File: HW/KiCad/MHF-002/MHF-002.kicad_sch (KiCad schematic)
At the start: 264 parts, among them J1 VGA, J10 I2C, J100 x, J101 x, J102 x, J103 x, J104 x, J105 x, J106 x, J107 +3V3, J108 GND, J109 +3V3, J11 + 5V -, J110 +5V, J111 GND, J112 GND, J12 Reset, J13 +5V, J14 GND, J15 AREF, J16 XTAL2, J17 SDcard, J18 XTAL1, J19 AVCC, J2 PS/2, J20 SDcardpins, J21 x, J22 x, J23 VIN 12V, J24 AND_B1, J25 AND_B2, J26 AND_C1, J27 AND_C2, J28 AND_D1, J29 AND_D2, J3 RCA, J30 AND_Dx, J31 AND_Cx, J32 AND_Bx, J33 NOTF, J34 NOTE, J35 NOTEx, J36 NOTFx, J37 x, J38 x, J39 x, J4 SysBus, J40 x, J41 x, J42 x, J43 x, J44 x, J45 x, J46 x, J47 x, J48 x, J49 x, J5 Micro, J50 x, J51 x, J52 x, J53 x, J54 x, J55 x, J56 x, J57 x, J58 x, J59 x, J6 SysBus, J60 x, J61 x, J62 x, J63 x, J64 x, J65 x, J66 x, J67 x, J68 x, J69 x, J7 SPI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

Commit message: external memory
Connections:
- net L4: now reaches M3.16 (A4), U6.12 (O4)
- net L5: now reaches M3.15 (A5), U6.15 (O5)
- net L6: now reaches M3.14 (A6), U6.16 (O6)
- net L7: now reaches M3.13 (A7), U6.19 (O7)
- net L3: now reaches M3.20 (A0), U6.2 (O0)
- net L2: now reaches M3.19 (A1), U6.5 (O1)
- net L1: now reaches M3.18 (A2), U6.6 (O2)
- net L0: now reaches M3.17 (A3), U6.9 (O3)
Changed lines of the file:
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@@
 	(wire
 		(pts
-			(xy 551.18 472.44) (xy 577.85 472.44)
+			(xy 551.18 472.44) (xy 769.62 472.44)
 		)
 		(stroke
@@
 	(wire
 		(pts
+			(xy 769.62 372.11) (xy 786.13 372.11)
+		)
+		(stroke
+			(width 0)
+			(type default)
+		)
+	)
+	(wire
+		(pts
 			(xy 472.44 347.98) (xy 478.79 347.98)
 		)
@@
 	(wire
 		(pts
-			(xy 783.59 372.11) (xy 786.13 372.11)
-		)
-		(stroke
-			(width 0)
-			(type default)
-		)
-	)
-	(wire
-		(pts
 			(xy 499.11 721.36) (xy 509.27 721.36)
 		)
@@
 	(wire
 		(pts
+			(xy 769.62 372.11) (xy 769.62 472.44)
+		)
+		(stroke
+			(width 0)
+			(type default)
+		)
+	)
+	(wire
+		(pts
 			(xy 763.27 367.03) (xy 786.13 367.03)
 		)
@@
 		)
 	)
+	(label "L7"
+		(at 763.27 349.25 0)
+		(effects
+			(font
+				(size 1.27 1.27)
+			)
+			(justify left bottom)
+		)
+	)
 	(label "A8"
 		(at 594.36 69.85 0)
@@
 		)
 	)
+	(label "L5"
+		(at 758.19 344.17 0)
+		(effects
+			(font
+				(size 1.27 1.27)
+			)
+			(justify left bottom)
+		)
+	)
 	(label "Shared_Address_A10"
 		(at 410.21 429.26 0)
@@
 		)
 	)
+	(label "L3"
+		(at 764.54 331.47 0)
+		(effects
+			(font
+				(size 1.27 1.27)
+			)
+			(justify left bottom)
+		)
+	)
 	(label "A_SHARE_GRANTED"
 		(at 689.61 88.9 0)
@@
 		)
 	)
+	(label "L6"
+		(at 762 346.71 0)
+		(effects
+			(font
+				(size 1.27 1.27)
+			)
+			(justify left bottom)
+		)
+	)
 	(label "A12"
 		(at 91.44 580.39 180)
@@
 		)
 	)
+	(label "L2"
+		(at 760.73 334.01 0)
+		(effects
+			(font
+				(size 1.27 1.27)
+			)
+			(justify left bottom)
+		)
+	)
 	(label "A12"
 		(at 594.36 74.93 0)
@@
 		)
 	)
+	(label "L0"
+		(at 753.11 339.09 0)
+		(effects
+			(font
+				(size 1.27 1.27)
+			)
+			(justify left bottom)
+		)
+	)
 	(label "A5"
 		(at 660.4 64.77 0)
@@
 		)
 	)
+	(label "L4"
+		(at 755.65 341.63 0)
+		(effects
+			(font
+				(size 1.27 1.27)
+			)
+			(justify left bottom)
+		)
+	)
 	(label "A16"
 		(at 689.61 78.74 0)
@@
 		(effects
 			(font
+				(size 1.27 1.27)
+			)
+			(justify left bottom)
+		)
+	)
+	(label "L1"
+		(at 756.92 336.55 0)
+		(effects
+			(font

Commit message: footprints for HandSoldering, some schema modifications
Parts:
- removed U4: 74HC165, Package_DIP:DIP-16_W7.62mm, symbol 74xx:74HC165
- added R44, R45: 10k, Resistor_SMD:R_0805_2012Metric_Pad1.20x1.40mm_HandSolder, symbol Device:R
- added U5: 74HC166, symbol 74xx:74LS166
- M3, M5: footprint Package_SO:TSOP-I-32_18.4x8mm_P0.5mm -> MHF:G_TSOP-I-32_18.4x8mm_HandSolder
- U1: footprint Package_QFP:TQFP-100_14x14mm_P0.5mm -> MHF:G_TQFP-100_14x14mm_HandSolder
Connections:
- net +5V: now also U5.16 (VCC), U5.9 (Clr)
- net 16MHz: now also U5.7 (Clk)
- net CTS: now also PB1.5 (Pin_5), U1.23 ((OC2A/PCINT4)PB4); no longer PE1.3 (Pin_3), U1.4 ((XCK0/AIN0)PE2)
- net GND: now also U5.6 (CE), U5.8 (GND)
- net PS2 Clock: now also R44.2; no longer JP56.2 (B)
- net PS2 Data: now also R45.2; no longer JP55.2 (B)
- net PS2-OE: now also PE1.3 (Pin_3), U1.4 ((XCK0/AIN0)PE2); no longer PB1.5 (Pin_5), U1.23 ((OC2A/PCINT4)PB4)
- net RTS: now also PB1.6 (Pin_6), U1.24 ((OC1A/PCINT5)PB5); no longer PE1.4 (Pin_4), U1.5 ((OC3A/AIN1)PE3)
- net Shared_data_D0: now also PL1.1 (Pin_1), U1.35 (PL0(ICP4)); no longer PF1.1 (Pin_1), U1.97 ((ADC0)PF0)
- net Shared_data_D1: now also PL1.2 (Pin_2), U1.36 (PL1(ICP5)); no longer PF1.2 (Pin_2), U1.96 ((ADC1)PF1)
- net Shared_data_D2: now also PL1.3 (Pin_3), U1.37 (PL2(T5)); no longer PF1.3 (Pin_3), U1.95 ((ADC2)PF2)
- net Shared_data_D3: now also PL1.4 (Pin_4), U1.38 (PL3(OC5A)); no longer PF1.4 (Pin_4), U1.94 ((ADC3)PF3)
- net Shared_data_D4: now also PL1.5 (Pin_5), U1.39 (PL4(OC5B)); no longer PF1.5 (Pin_5), U1.93 ((ADC4/TCK)PF4)
- net Shared_data_D5: now also PL1.6 (Pin_6), U1.40 (PL5(OC5C)); no longer PF1.6 (Pin_6), U1.92 ((ADC5/TMS)PF5)
- net Shared_data_D6: now also PL1.7 (Pin_7), U1.41 (PL6); no longer PF1.7 (Pin_7), U1.91 ((ADC6/TDO)PF6)
- net Shared_data_D7: now also PL1.8 (Pin_8), U1.42 (PL7); no longer PF1.8 (Pin_8), U1.90 ((ADC7/TDI)PF7)
- net VGA Latch: now also U5.15 (PE)
- net VGA data 0: now also PF1.1 (Pin_1), U1.97 ((ADC0)PF0), U5.2 (A); no longer PL1.1 (Pin_1), U1.35 (PL0(ICP4))
- net VGA data 1: now also PF1.2 (Pin_2), U1.96 ((ADC1)PF1), U5.3 (B); no longer PL1.2 (Pin_2), U1.36 (PL1(ICP5))
- net VGA data 2: now also PF1.3 (Pin_3), U1.95 ((ADC2)PF2), U5.4 (C); no longer PL1.3 (Pin_3), U1.37 (PL2(T5))
- net VGA data 3: now also PF1.4 (Pin_4), U1.94 ((ADC3)PF3), U5.5 (D); no longer PL1.4 (Pin_4), U1.38 (PL3(OC5A))
- net VGA data 4: now also PF1.5 (Pin_5), U1.93 ((ADC4/TCK)PF4), U5.10 (E); no longer N1.2, PL1.5 (Pin_5), U1.39 (PL4(OC5B))
- net VGA data 5: now also PF1.6 (Pin_6), U1.92 ((ADC5/TMS)PF5), U5.11 (F); no longer PL1.6 (Pin_6), U1.40 (PL5(OC5C))
- net VGA data 6: now also PF1.7 (Pin_7), U1.91 ((ADC6/TDO)PF6), U5.12 (G); no longer PL1.7 (Pin_7), U1.41 (PL6)
- net VGA data 7: now also PF1.8 (Pin_8), U1.90 ((ADC7/TDI)PF7), U5.14 (H); no longer PL1.8 (Pin_8), U1.42 (PL7)
- net VSyncVGA: now also N1.2
- net X16: now also PE1.4 (Pin_4), U1.5 ((OC3A/AIN1)PE3); no longer PB1.6 (Pin_6), U1.24 ((OC1A/PCINT5)PB5)
- net at U9.1 (S): now also U5.13 (Qh)
- new net: JP55.2 (B), R45.1
- new net: JP56.2 (B), R44.1
- no-connect marks 120 -> 119
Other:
- note added: "PB7 is usual Arduino Mega SYSTEM_LED - with VGA it will shine full time"
- moved on the sheet: C5, J15, U2E

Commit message: +footprints
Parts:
- added JP15: TX340, Jumper:SolderJumper-2_P1.3mm_Open_RoundedPad1.0x1.5mm, symbol Jumper:SolderJumper_2_Open
- added JP16: RX340, Jumper:SolderJumper-2_P1.3mm_Open_RoundedPad1.0x1.5mm, symbol Jumper:SolderJumper_2_Open
- added JP17: CTS340, Jumper:SolderJumper-2_P1.3mm_Open_RoundedPad1.0x1.5mm, symbol Jumper:SolderJumper_2_Open
- added JP18: DTR340, Jumper:SolderJumper-2_P1.3mm_Open_RoundedPad1.0x1.5mm, symbol Jumper:SolderJumper_2_Open
- added JP19: RTS340, Jumper:SolderJumper-2_P1.3mm_Open_RoundedPad1.0x1.5mm, symbol Jumper:SolderJumper_2_Open
- added JP20: USB_GND, MHF:G_rework_jumper_2.54mm, symbol MHF:ReworkJumper_2_Bridged
- added M1: CP2102, MHF:G_CP2102, symbol MHF:G_CP2102
- C9: footprint Capacitor_SMD:C_0603_1608Metric_Pad1.08x0.95mm_HandSolder -> Capacitor_THT:C_Disc_D3.0mm_W2.0mm_P2.50mm
- J2: footprint other.pretty:J_Mini-DIN-6 -> MHF:J_Mini-DIN-6; symbol Connector:Mini-DIN-6 -> MHF:Mini-DIN-6
- J3: footprint Gilhad:CUI_RCJ-047_Yellow -> MHF:CUI_RCJ-047_Yellow; symbol Connector:Conn_Coaxial -> MHF:Conn_Coaxial
- U10, U11, U12: footprint Package_SO:SOIC-20W_7.5x12.8mm_P1.27mm -> MHF:G_SOIC-20W_7.5x12.8mm_P1.27mm_HandSolder
- U5: footprint (none) -> MHF:G_SOIC-16_3.9x9.9mm_HandSolder
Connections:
- net CTS: now also JP17.2 (B); no longer U13.9 (~{CTS})
- net GND: now also JP20.2 (B); no longer J5.5 (GND), J5.6 (Shield)
- net M8RXD: now also JP16.2 (B); no longer U13.3 (RXD)
- net M8TXD: now also JP15.2 (B); no longer U13.2 (TXD)
- net RTS: now also JP19.2 (B); no longer U13.14 (~{RTS})
- net at C9.2, R28.2: now also JP18.2 (B); no longer U13.13 (~{DTR})
- new net: JP18.1 (A), U13.13 (~{DTR})
- new net: J5.5 (GND), J5.6 (Shield), JP20.1 (A)
- new net: JP17.1 (A), U13.9 (~{CTS})
- new net: JP15.1 (A), U13.2 (TXD)
- new net: JP19.1 (A), U13.14 (~{RTS})
- new net: JP16.1 (A), U13.3 (RXD)

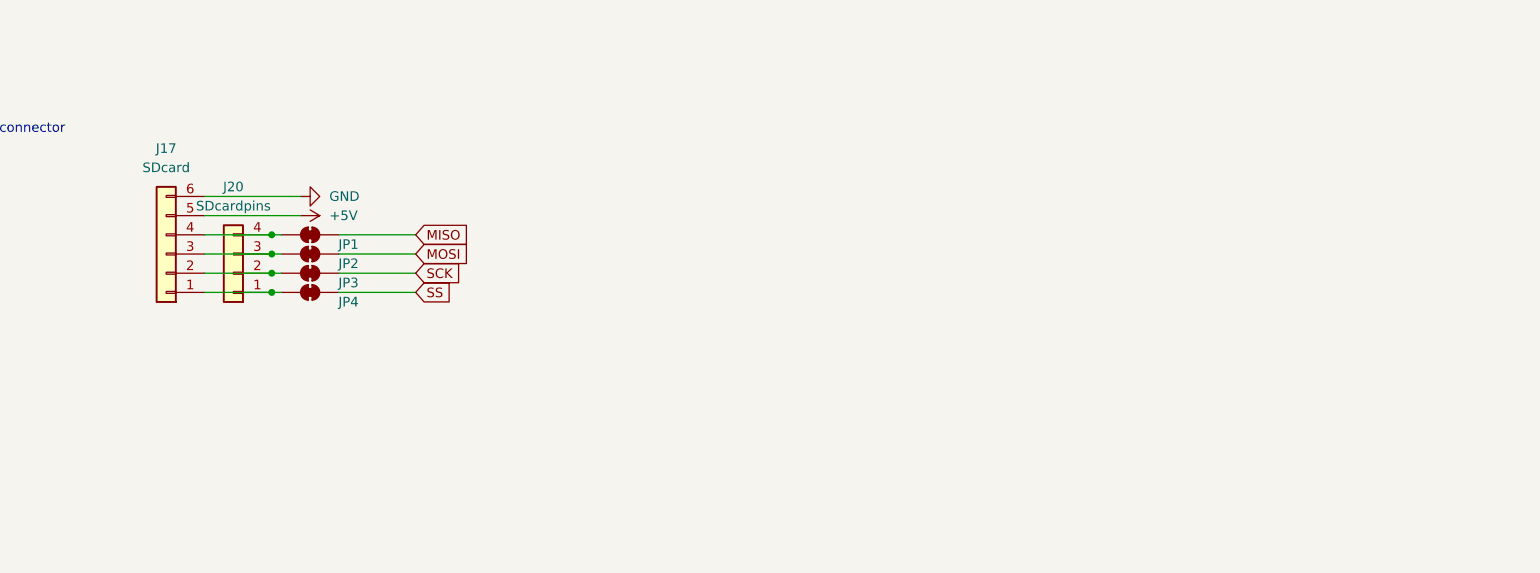
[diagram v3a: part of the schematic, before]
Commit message: +cp2102 +SDCard
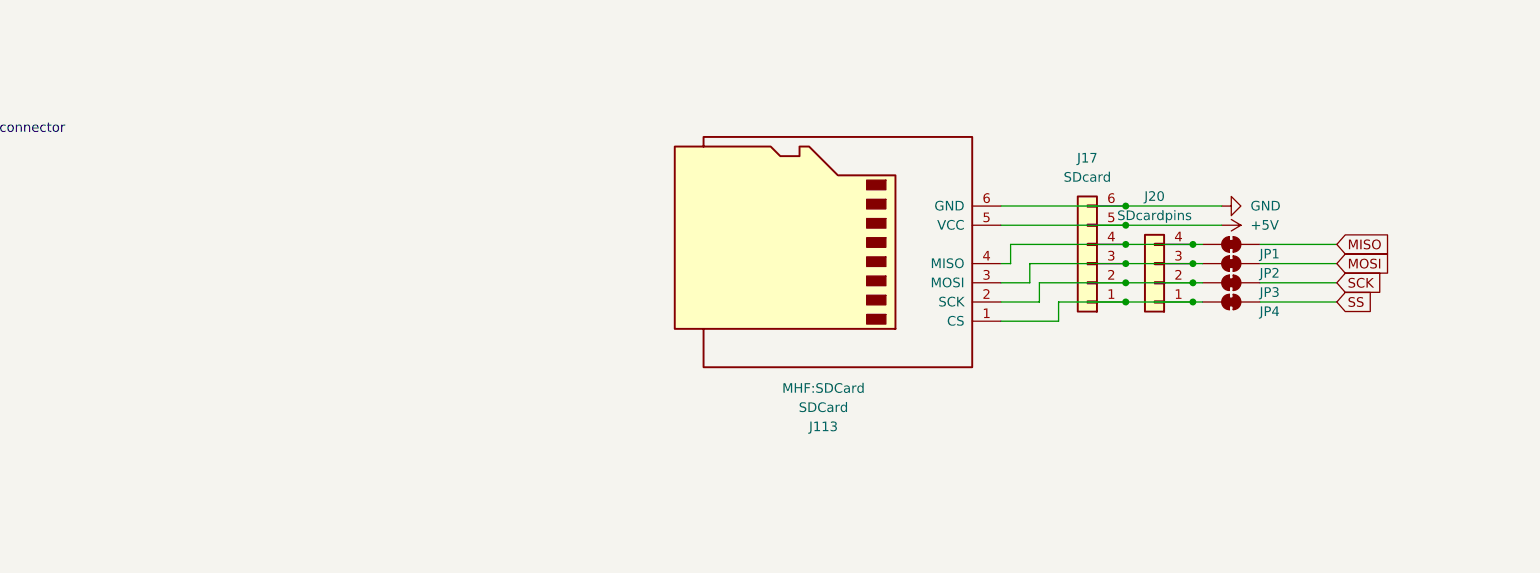
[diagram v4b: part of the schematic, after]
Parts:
- added J113: SDCard, MHF:SDCard, symbol MHF:SDCard
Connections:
- net +5V: now also J113.5 (VCC)
- net GND: now also J113.6 (GND)
- net at J17.3 (Pin_3), J20.3 (Pin_3), JP2.1 (A): now also J113.3 (MOSI)
- net at J17.4 (Pin_4), J20.4 (Pin_4), JP1.1 (A): now also J113.4 (MISO)
- net at J17.1 (Pin_1), J20.1 (Pin_1), JP4.1 (A): now also J113.1 (CS)
- net at J17.2 (Pin_2), J20.2 (Pin_2), JP3.1 (A): now also J113.2 (SCK)
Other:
- moved on the sheet: J17, J20, JP1, JP2, JP3, JP4

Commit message: more small fixes
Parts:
- removed U6: 74AHC373, Package_SO:TSSOP-20_4.4x6.5mm_P0.65mm, symbol 74xx:74AHC373
- added JP21: TX2102, Jumper:SolderJumper-2_P1.3mm_Open_RoundedPad1.0x1.5mm, symbol Jumper:SolderJumper_2_Open
- added JP22: RX2102, Jumper:SolderJumper-2_P1.3mm_Open_RoundedPad1.0x1.5mm, symbol Jumper:SolderJumper_2_Open
- added JP23: CTS2102, Jumper:SolderJumper-2_P1.3mm_Open_RoundedPad1.0x1.5mm, symbol Jumper:SolderJumper_2_Open
- added JP24: DTR2102, Jumper:SolderJumper-2_P1.3mm_Open_RoundedPad1.0x1.5mm, symbol Jumper:SolderJumper_2_Open
- added JP25: RTS2102, Jumper:SolderJumper-2_P1.3mm_Open_RoundedPad1.0x1.5mm, symbol Jumper:SolderJumper_2_Open
- added JP26: PS/2, Connector_PinHeader_2.54mm:PinHeader_1x02_P2.54mm_Vertical, symbol Connector_Generic:Conn_01x02
- added JP27: VGA, Connector_PinHeader_2.54mm:PinHeader_1x06_P2.54mm_Vertical, symbol Connector_Generic:Conn_01x06
- added JP28: RCA, Connector_PinHeader_2.54mm:PinHeader_1x02_P2.54mm_Vertical, symbol Connector_Generic:Conn_01x02
- added U4: 74AHC573, Package_SO:TSSOP-20_4.4x5mm_P0.5mm, symbol 74xx:74LS573
- C1: value 100 pF -> 10 nF
- J113: footprint MHF:SDCard -> SDCard:SDCard
- Q1: value BC107 -> S8050
- R1: value 3k3/22k -> 20k
- S1: symbol Arduino Mega 2560:TS06-667-30-BK-100-G-SMT-TR -> Switch:SW_MEC_5E
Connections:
- net +5V: now also M1.8 (+5V), U4.20 (VCC)
- net ALE: now also U4.11 (Load)
- net Blue: now also JP27.3 (Pin_3)
- net CTS: now also JP23.2 (B)
- net GND: now also M1.9 (GND), S1.3 (K), S1.4 (A), JP27.6 (Pin_6), JP28.2 (Pin_2), U4.1 (OE), U4.10 (GND); no longer S1.1, S1.2, S1.5
- net Green: now also JP27.4 (Pin_4)
- net L0: now also U4.16 (Q3)
- net L1: now also U4.17 (Q2)
- net L2: now also U4.18 (Q1)
- net L3: now also U4.19 (Q0)
- net L4: now also U4.15 (Q4)
- net L5: now also U4.14 (Q5)
- net L6: now also U4.13 (Q6)
- net L7: now also U4.12 (Q7)
- net M8RXD: now also JP22.2 (B)
- net M8TXD: now also JP21.2 (B)
- net PS2 Data: now also JP26.2 (Pin_2)
- net RCA_Output: now also JP28.1 (Pin_1)
- net RTS: now also JP25.2 (B)
- net Red: now also JP27.5 (Pin_5)
- net Reset: now also S1.1, S1.2; no longer S1.3, S1.4
- net XAD0: now also U4.5 (D3)
- net XAD1: now also U4.4 (D2)
- net XAD2: now also U4.3 (D1)
- net XAD3: now also U4.2 (D0)
- net XAD4: now also U4.6 (D4)
- net XAD5: now also U4.7 (D5)
- net XAD6: now also U4.8 (D6)
- net XAD7: now also U4.9 (D7)
- net at J1.13, R14.1: now also JP27.2 (Pin_2)
- net at J1.14, R15.1: now also JP27.1 (Pin_1)
- net DTR: now reaches C9.2, JP18.2 (B), R28.2
- net DTR: now also JP24.2 (B)
- net at M1.3 (RTS): now also JP25.1 (A)
- net at M1.4 (CTS): now also JP23.1 (A)
- net at M1.5 (DTR): now also JP24.1 (A)
- net at M1.6 (RXD): now also JP22.1 (A)
- net at M1.7 (TXD): now also JP21.1 (A)
- net at J2.5, R13.1, U2.1: now also JP26.1 (Pin_1)
- no-connect marks 119 -> 126
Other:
- moved on the sheet: C12, C9, D2, J113, J12, R14, R15, R26, R28

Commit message: +Switch
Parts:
- added LED10: Reset, LED_SMD:LED_0805_2012Metric, symbol Device:LED
- added LED9: SYSTEM, LED_SMD:LED_0805_2012Metric, symbol Device:LED
- added R46, R47: 10k, Resistor_SMD:R_0805_2012Metric_Pad1.20x1.40mm_HandSolder, symbol Device:R
- C12: footprint Capacitor_SMD:C_0603_1608Metric_Pad1.08x0.95mm_HandSolder -> Capacitor_THT:C_Disc_D3.0mm_W2.0mm_P2.50mm
- C13, C14: value 100n -> 22p
- J113: footprint SDCard:SDCard -> MHF:SDCard
- JP20: footprint MHF:G_rework_jumper_2.54mm -> MHF:G_Rework_Jumper_Bridged_2.54mm; symbol MHF:ReworkJumper_2_Bridged -> MHF:Rework_Jumper_2_Bridged
- S1: footprint Arduino Mega 2560:SW_TS06-667-30-BK-100-G-SMT-TR -> MHF:G_Arduino_switch; symbol Switch:SW_MEC_5E -> MHF:Arduino_Switch
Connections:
- net +5V: now also R47.2
- net GND: now also LED9.1 (K)
- net Reset: now also LED10.1 (K)
- net VGA Latch: now also R46.2
- new net: LED10.2 (A), R47.1
- new net: LED9.2 (A), R46.1

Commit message: fixing small problems
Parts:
- added JP30: USB_PWR, MHF:G_Rework_Jumper_Bridged_2.54mm, symbol MHF:Rework_Jumper_2_Bridged
- added JP31: USB_D+, MHF:G_Rework_Jumper_Bridged_2.54mm, symbol MHF:Rework_Jumper_2_Bridged
- added JP32: USB_D-, MHF:G_Rework_Jumper_Bridged_2.54mm, symbol MHF:Rework_Jumper_2_Bridged
- C1, C10, C11, C12, C13, C14, C15, C16, C2, C3, C4, C5, C6, C7, C8, C9, Cx1, Cx10, Cx11, Cx12, Cx13, Cx2, Cx3, Cx4, Cx5, Cx6, Cx7, Cx8, Cx9: symbol Device:C -> MHF:C
- Cx14, Cx15: symbol Device:C_Polarized -> MHF:C_Polarized
- D1: symbol Diode:1N4001 -> MHF:1N4001
- D2, D3: symbol Device:D -> MHF:D
- F1: symbol Device:Polyfuse -> MHF:Polyfuse
- H5, H6, H7, H8: symbol Mechanical:MountingHole -> MHF:MountingHole
- J1: symbol Connector:DE15_Socket_HighDensity_MountingHoles -> MHF:DE15_Socket_HighDensity_MountingHoles
- J10, J20: symbol Connector_Generic:Conn_01x04 -> MHF:Conn_01x04
- J100, J101, J102, J103, J104, J105, J106, J107, J108, J109, J110, J111, J112, J12, J13, J14, J15, J16, J18, J19, J21, J22, J24, J25, J26, J27, J28, J29, J30, J31, J32, J33, J34, J35, J36, J37, J38, J39, J40, J41, J42, J43, J44, J45, J46, J47, J48, J49, J50, J51, J52, J53, J54, J55, J56, J57, J58, J59, J60, J61, J62, J63, J64, J65, J66, J67, J68, J69, J70, J71, J72, J73, J74, J75, J76, J77, J78, J79, J80, J81, J82, J83, J84, J85, J86, J87, J88, J89, J90, J91, J92, J93, J94, J95, J96, J97, J98, J99: symbol PCM_Gilhad_symbols:Conn_01x01 -> MHF:Conn_01x01
- J11: symbol Connector_Generic:Conn_02x03_Odd_Even -> MHF:Conn_02x03_Odd_Even
- J17, J7, J9, JP27, PG1: symbol Connector_Generic:Conn_01x06 -> MHF:Conn_01x06
- J23: symbol Connector:Barrel_Jack_Switch -> MHF:Barrel_Jack_Switch
- J4, J6: symbol Connector_Generic:Conn_02x32_Odd_Even -> MHF:Conn_02x32_Odd_Even
- J5: symbol Connector:USB_B_Micro -> MHF:USB_B_Micro
- J8: symbol Connector:AVR-ISP-6 -> MHF:AVR-ISP-6
- JP1, JP10, JP11, JP12, JP13, JP14, JP2, JP3, JP4, JP5, JP6, JP7, JP8, JP9, JP91: symbol Jumper:SolderJumper_2_Bridged -> MHF:SolderJumper_2_Bridged
- JP100, JP102, JP103, JP104, JP105, JP106, JP107, JP92, JP94, JP95, JP98, JP99: symbol Jumper:SolderJumper_3_Open -> MHF:SolderJumper_3_Open
- JP15, JP16, JP17, JP18, JP19, JP21, JP22, JP23, JP24, JP25, JP55, JP56: symbol Jumper:SolderJumper_2_Open -> MHF:SolderJumper_2_Open
- JP26, JP28: symbol Connector_Generic:Conn_01x02 -> MHF:Conn_01x02
- LED1, LED10, LED2, LED3, LED4, LED5, LED6, LED7, LED8, LED9: symbol Device:LED -> MHF:LED
- M3, M5: symbol Memory_RAM:AS6C1008-xxST -> MHF:AS6C1008-xxST
- N1, N3: symbol Device:NetTie_2 -> MHF:NetTie_2
- PA1, PB1, PC1, PD1, PE1, PF1, PH1, PJ1, PK1, PL1: symbol Connector_Generic:Conn_01x08 -> MHF:Conn_01x08
- Q1: symbol Transistor_BJT:S8050 -> MHF:S8050
- R1, R10, R11, R12, R13, R14, R15, R16, R17, R18, R19, R2, R20, R21, R22, R23, R24, R25, R26, R27, R28, R29, R3, R30, R31, R32, R33, R34, R35, R36, R37, R38, R39, R4, R40, R41, R42, R43, R44, R45, R46, R47, R5, R6, R7, R8, R9: symbol Device:R -> MHF:R
- U1: symbol Arduino Mega 2560:ATMEGA2560-16AU -> MHF:ATMEGA2560-16AU
- U10, U11, U12: symbol 74xx:74HC245 -> MHF:74HC245
- U13: symbol Interface_USB:CH340G -> MHF:CH340G
- U14: symbol Regulator_Linear:AMS1117-5.0 -> MHF:AMS1117-5.0
- U15: symbol Regulator_Linear:AMS1117-3.3 -> MHF:AMS1117-3.3
- U2: symbol 74xx:74HC14 -> MHF:74HC14
- U3: value 74LS08 -> 74HC08; symbol 74xx:74LS08 -> MHF:74HC08
- U4: symbol 74xx:74LS573 -> MHF:74HC573
- U5: symbol 74xx:74LS166 -> MHF:74HC166
- U7, U8: symbol 74xx:74HCT595 -> MHF:74HC595
- U9: symbol 74xx:74LS157 -> MHF:74HC157
- Y1, Y2: symbol Device:Crystal -> MHF:Crystal
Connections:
- net at R24.2: now also JP31.2 (B); no longer J5.3 (D+)
- net at J5.1 (VBUS): now also JP30.1 (A); no longer F1.2
- net at J5.2 (D-): now also JP32.1 (A); no longer R25.2
- new net: JP32.2 (B), R25.2
- new net: F1.2, JP30.2 (B)
- new net: J5.3 (D+), JP31.1 (A)
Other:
- moved on the sheet: F1, R24, R25
